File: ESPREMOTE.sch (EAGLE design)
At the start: 38 parts, among them IC1 ESP12SMT, J1 2.1MM DC Jack, Q1 2N7002, Q2 2N7002, Q3 2N7002, Q4 2N7002

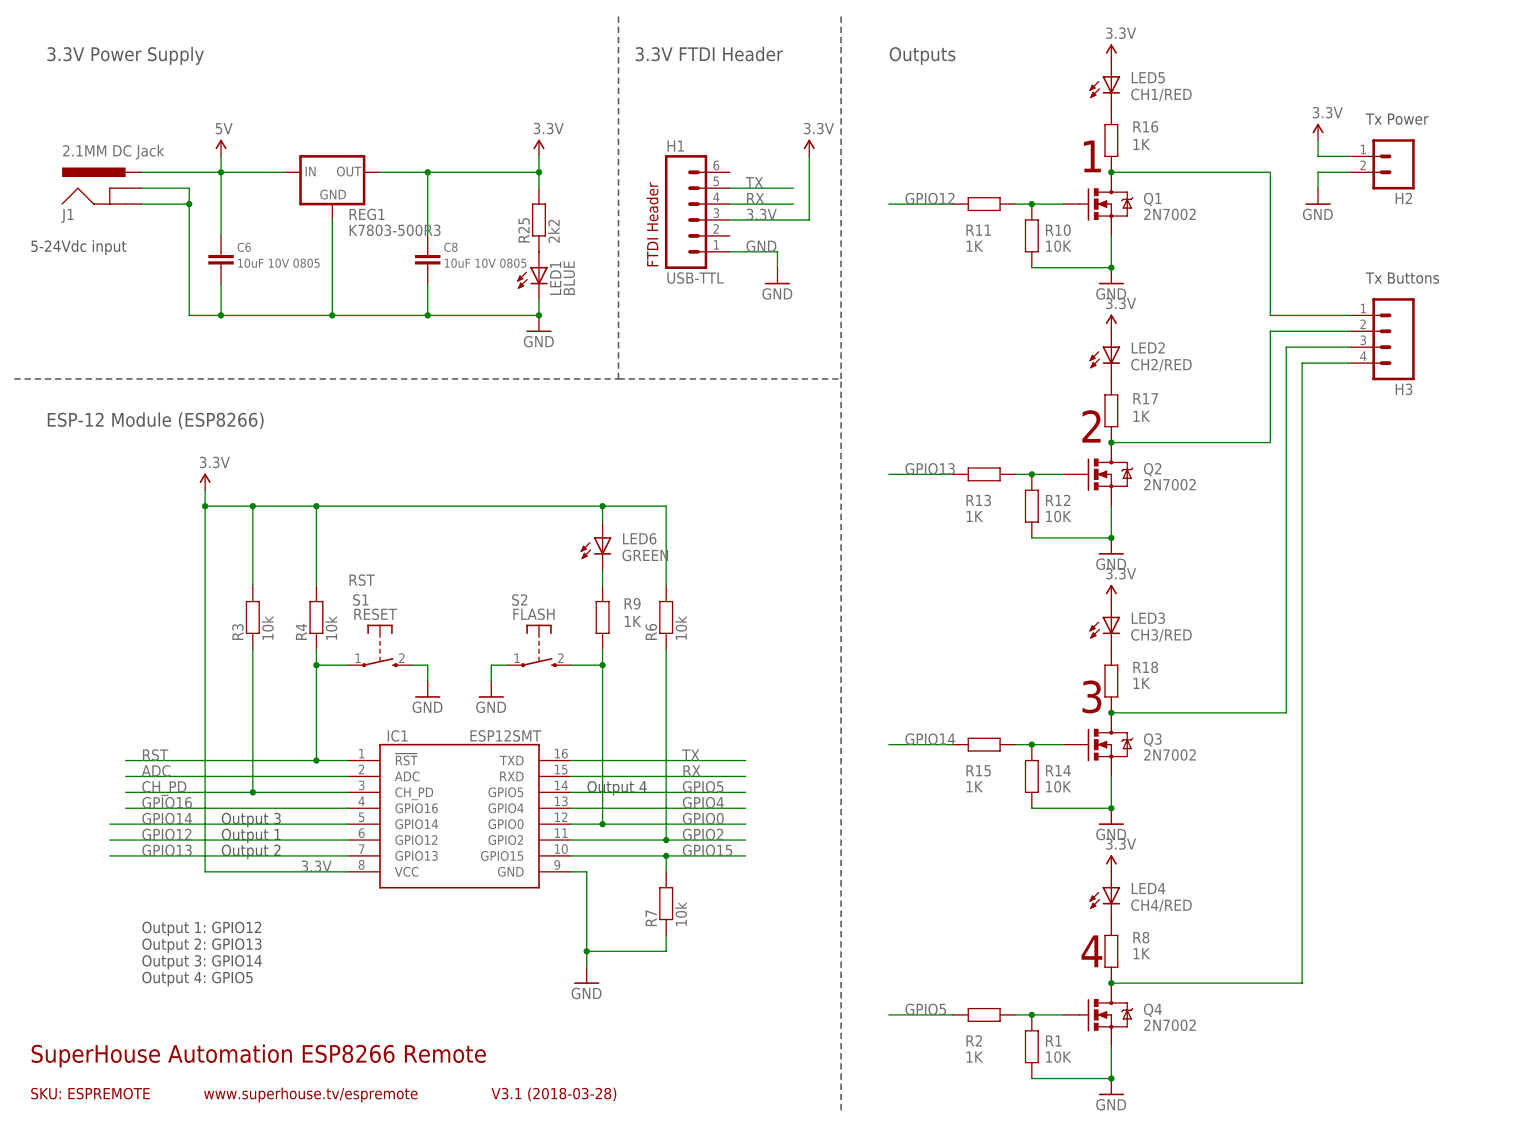
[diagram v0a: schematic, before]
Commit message: Added reed relays
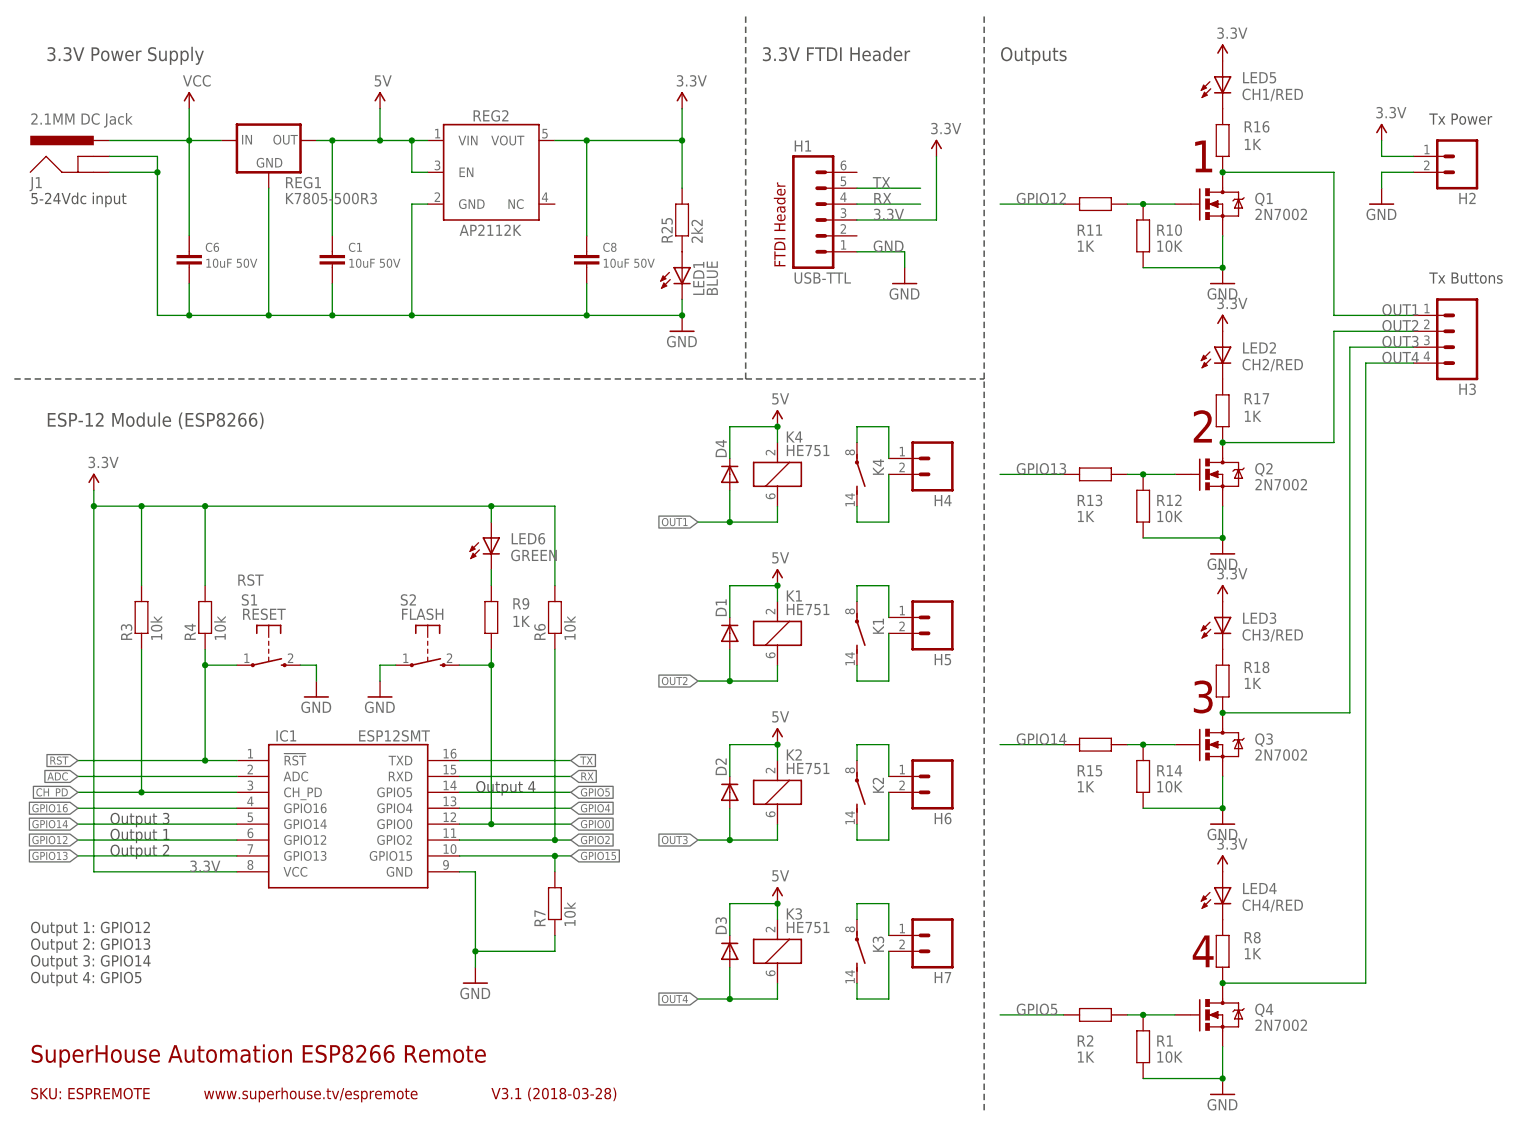
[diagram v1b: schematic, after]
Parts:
- added C1: 10uF 50V, freetronics-jon:C-EUC0805
- added D1, D2, D3, D4: (no value), SparkFun:DIODESMA
- added H4, H5, H6, H7: (no value), freetronics-jon:M02PTH
- added K1, K2, K3, K4: HE751, relay:HE751
- added REG2: AP2112KSOT25, freetronics-jon:AP2112KSOT25
- C6, C8: value 10uF 10V 0805 -> 10uF 50V
- REG1: value K7803-500R3 -> K7805-500R3
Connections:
- new net N$12: H4.2, K42.S
- new net N$13: H7.1, K32.P
- new net N$14: H7.2, K32.S
- new net N$8: H4.1, K42.P
- new net OUT1: D4.A, H3.1, K41.2, Q1.D, R16.2
- new net OUT2: D1.A, H3.2, K11.2, Q2.D, R17.2
- new net OUT3: D2.A, H3.3, K21.2, Q3.D, R18.2
- new net OUT4: D3.A, H3.4, K31.2, Q4.D, R8.2
- new net VCC: C6.1, J1.PWR, REG1.IN
- net 3.3V: now also REG2.VOUT; no longer REG1.OUT
- net 5V: now also C1.1, D1.C, D2.C, D3.C, D4.C, K11.1, K21.1, K31.1, K41.1, REG1.OUT, REG2.EN, REG2.VIN; no longer C6.1, J1.PWR, REG1.IN
- net GND: now also C1.2, REG2.GND
- net N$3: now also H5.1, K12.P; no longer H3.2, Q2.D, R17.2
- net N$5: now also H5.2, K12.S; no longer H3.1, Q1.D, R16.2
- net N$6: now also H6.1, K22.P; no longer H3.4, Q4.D, R8.2
- net N$9: now also H6.2, K22.S; no longer H3.3, Q3.D, R18.2
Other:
- moved on the sheet: C6, C8, H1, H2, H3, IC1, J1, LED1, LED2, LED3, LED4, LED5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
